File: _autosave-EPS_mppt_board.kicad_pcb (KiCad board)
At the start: 6 copper layers, 90 x 96 mm, 243 parts, among them J1 Conn_01x04_Pin, J2 ESQT-126-X-X-Q-X, J3 M80-5400642, J4 M80-5400642, J5 M80-5400642, J6 M80-5400642, Q10 NMOS, Q11 NMOS, Q12 NMOS, Q13 NMOS, Q14 NMOS, Q15 SIR5607DP-T1-RE3, Q16 SIR5607DP-T1-RE3, Q17 SIR5607DP-T1-RE3, Q4 NMOS, Q5 NMOS, Q6 NMOS, Q7 NMOS, Q8 NMOS, Q9 NMOS, U1 LTC4412xS6, U10 LTC4162IUFD-LADM_PBF, U11 MR20H40, U12 TCAN334, U13 TCA9548AMRGER, U15 INA3221, U16 TPS259470ARPWR, U17 TPS259470ARPWR, U18 TPS259470ARPWR, U19 LTC3633AIUFDPBF, U2 TPS259470ARPWR, U20 STM32L476RGTx, U3 TPS62177DQCR, U4 LTC4412xS6, U5 LTC2965HDD-PBF, U6 TPS3823A-33DBVR, U7 LTC4162IUFD-LADM_PBF, U8 LTC4162IUFD-LADM_PBF, U9 LTC4162IUFD-LADM_PBF, Y1 8 MHZ Oscillator

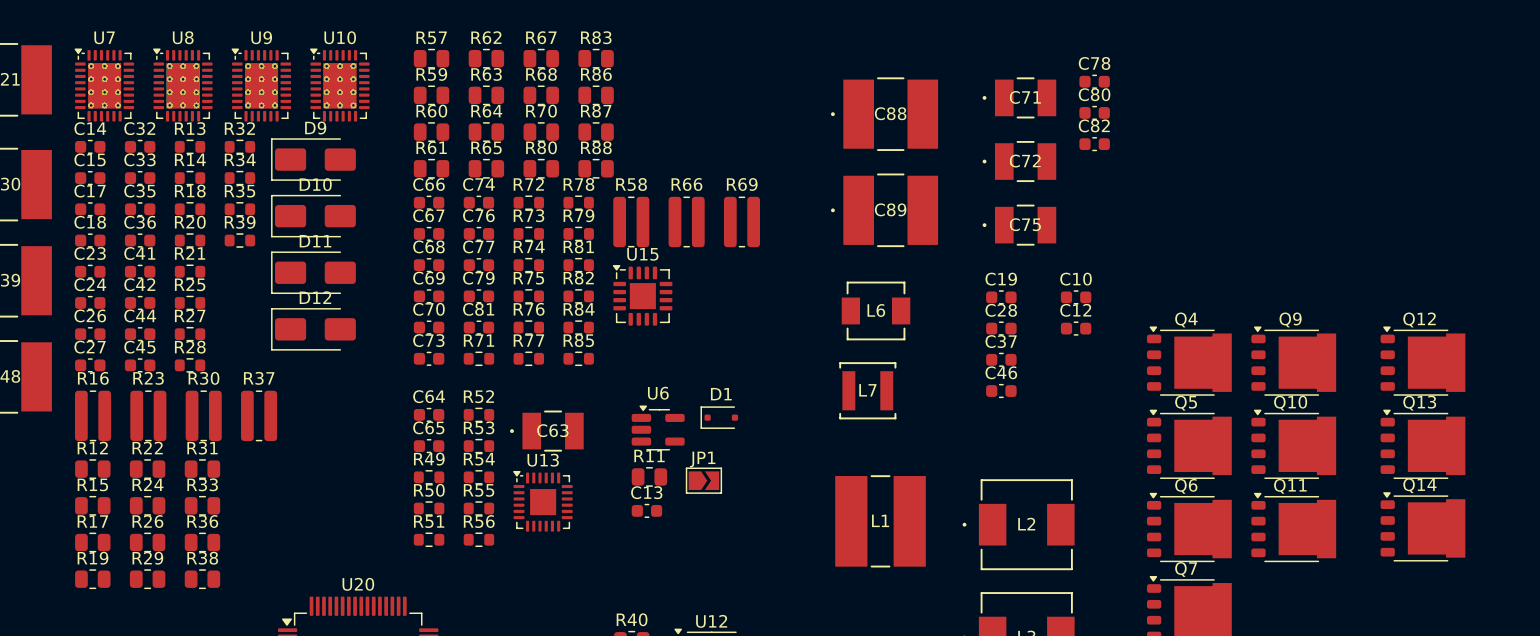
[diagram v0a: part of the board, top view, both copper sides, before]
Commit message: Added connectors to schematic
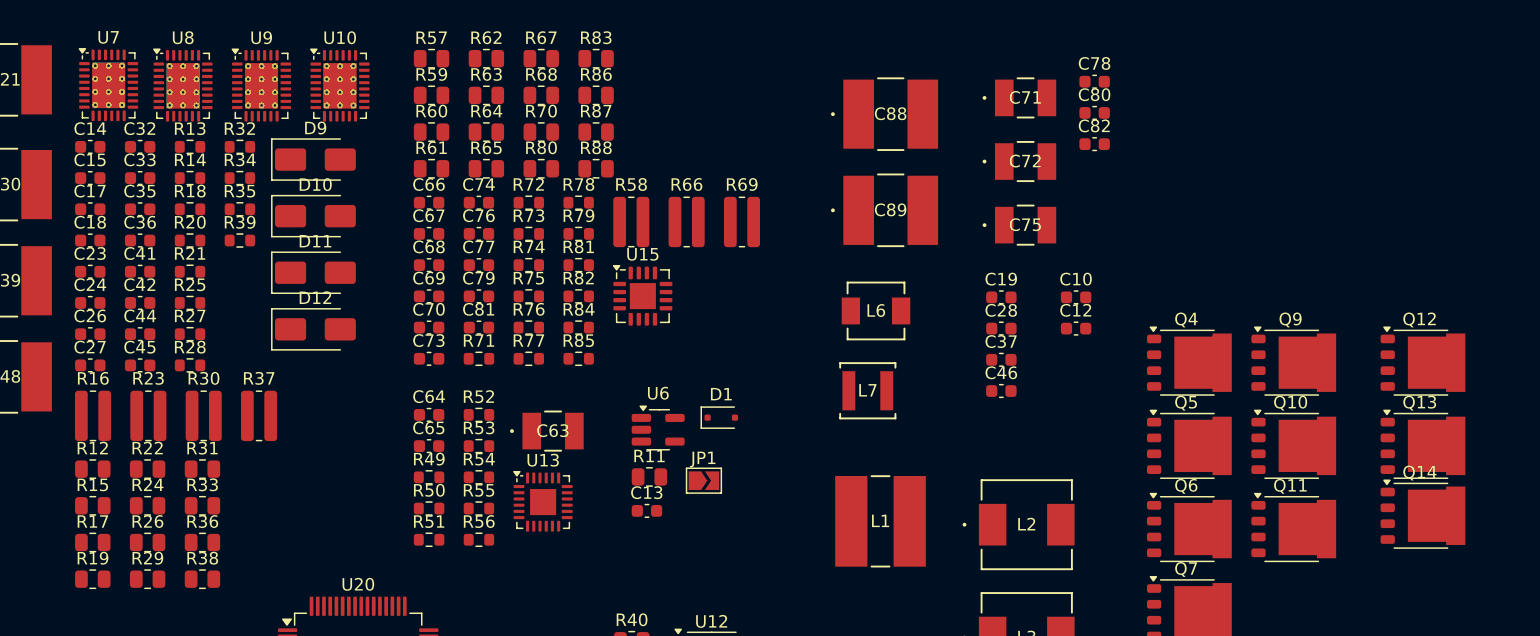
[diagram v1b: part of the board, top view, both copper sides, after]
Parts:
- moved Q14 1.02 mm to (85.0, 83.6)
- moved U7 0.33 mm to (-20.5, 49.0)
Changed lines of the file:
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@@
 	(footprint "Package_TO_SOT_SMD:LFPAK56"
 		(layer "F.Cu")
-		(at 85.015 84.65)
+		(at 85.015 83.63)
 		(descr "LFPAK56 https://assets.nexperia.com/documents/outline-drawing/SOT669.pdf")
 		(tags "LFPAK56 SOT-669 Power-SO8")
@@
 	(footprint "Package_DFN_QFN:QFN-28-1EP_4x5mm_P0.5mm_EP2.65x3.65mm_ThermalVias"
 		(layer "F.Cu")
-		(at -20.825 49.06)
+		(at -20.5 49.025)
 		(descr "QFN, 28 Pin (http://www.analog.com/media/en/technical-documentation/data-sheets/3555fe.pdf#page=32), generated with kicad-footprint-generator ipc_noLead_generator.py")
 		(tags "QFN NoLead")
